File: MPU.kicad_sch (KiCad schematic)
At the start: 105 parts, among them J3 Conn_01x08_Female, J4 Conn_01x08_Female, J5 Conn_01x08_Female, J6 Conn_01x08_Female, K1 G5NB-1A, K2 G5NB-1A, K3 G5NB-1A, K4 G5NB-1A, Q1 C1815, Q10 7002_GSD, Q11 7002_GSD, Q12 7002_GSD, Q13 7002_GSD, Q14 7002_GSD, Q15 7002_GSD, Q16 7002_GSD, Q17 7002_GSD, Q2 C1815, Q3 C1815, Q4 C1815, Q5 C1815, Q6 7002_GSD, Q7 7002_GSD, Q8 7002_GSD, Q9 7002_GSD, U1 BP, U4 LM1117-3.3, U5 PC817, U6 PC817, U7 PC817, U8 PC817

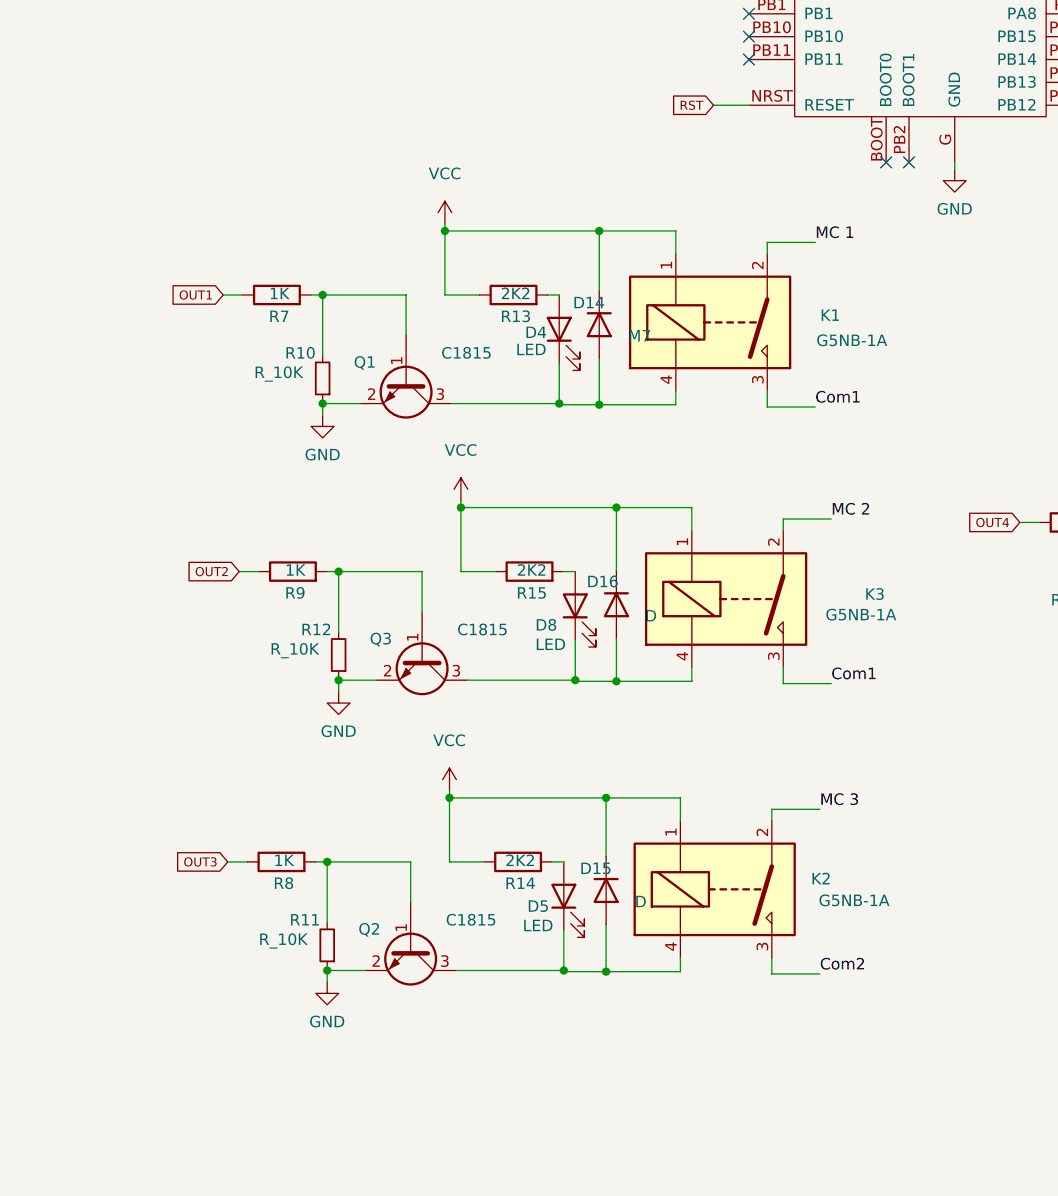
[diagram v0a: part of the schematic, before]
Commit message: schematic tao mot sheet output
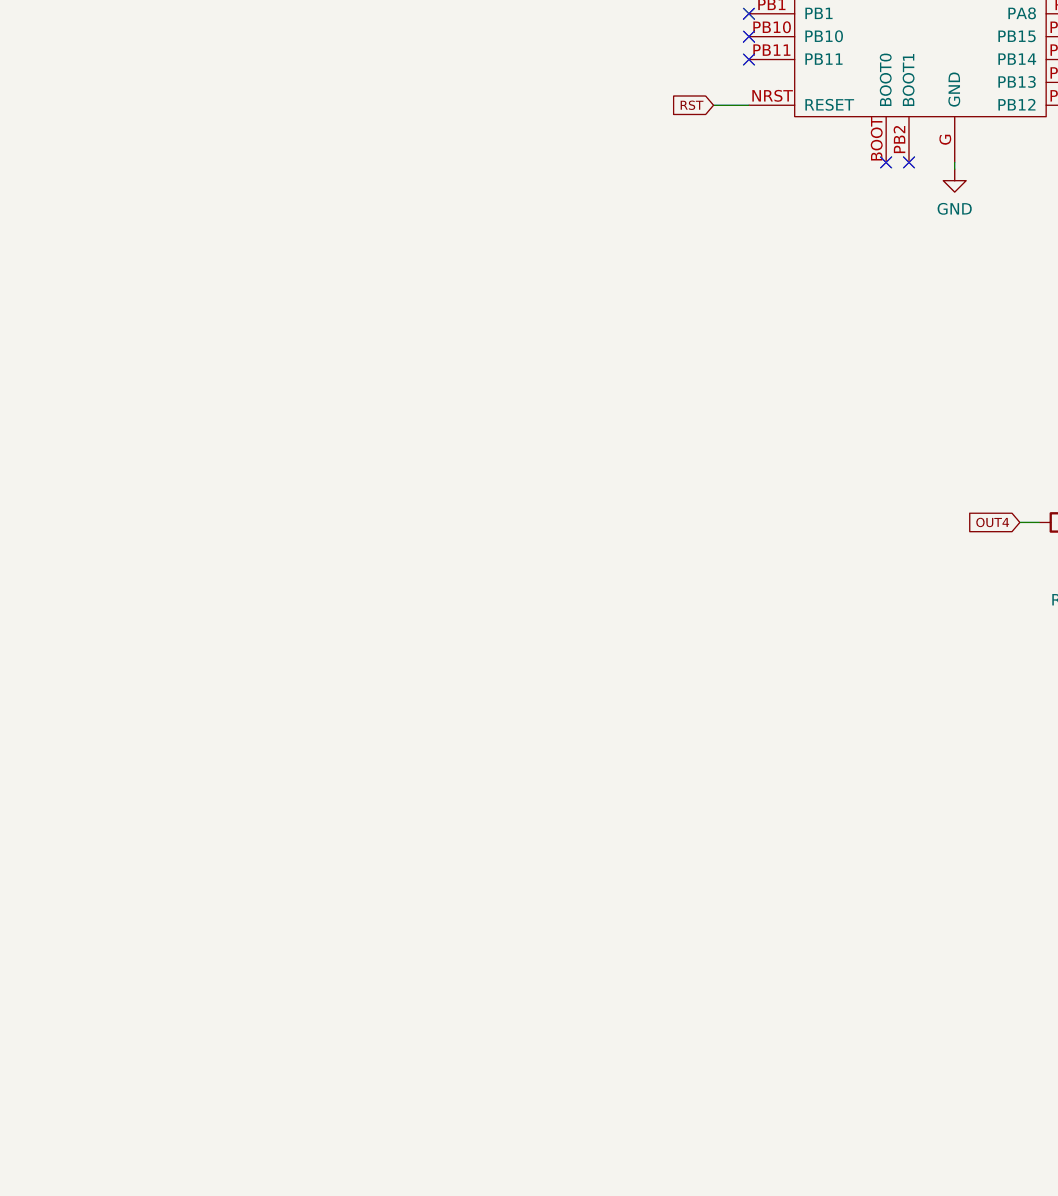
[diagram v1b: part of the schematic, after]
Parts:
- removed D14: M7, Diode_SMD:D_SMA, symbol Device:D
- removed D15, D16: D, Diode_SMD:D_SMA, symbol Device:D
- removed D4, D5, D8: LED, LED_SMD:LED_0805_2012Metric_Pad1.15x1.40mm_HandSolder, symbol Device:LED
- removed K1, K2, K3: G5NB-1A, My Footprint:G5NB-1A, symbol My_Device:G5NB-1A
- removed Q1, Q2, Q3: C1815, Package_TO_SOT_SMD:SOT-23, symbol My_Device:C1815
- removed R10, R11: R_10K, Resistor_SMD:R_0805_2012Metric_Pad1.20x1.40mm_HandSolder, symbol Device:R_Small
- removed R12: R_10K, My Footprint:R_0805_2012Metric_Pad1.20x1.40mm_HandSolder, symbol Device:R_Small
- removed R13, R14, R15: 2K2, Resistor_SMD:R_0805_2012Metric_Pad1.20x1.40mm_HandSolder, symbol Device:R
- removed R7, R8, R9: 1K, Resistor_SMD:R_0805_2012Metric_Pad1.20x1.40mm_HandSolder, symbol Device:R
